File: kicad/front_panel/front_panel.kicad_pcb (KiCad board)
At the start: 2 copper layers, 196.9 x 58.7 mm, 12 parts

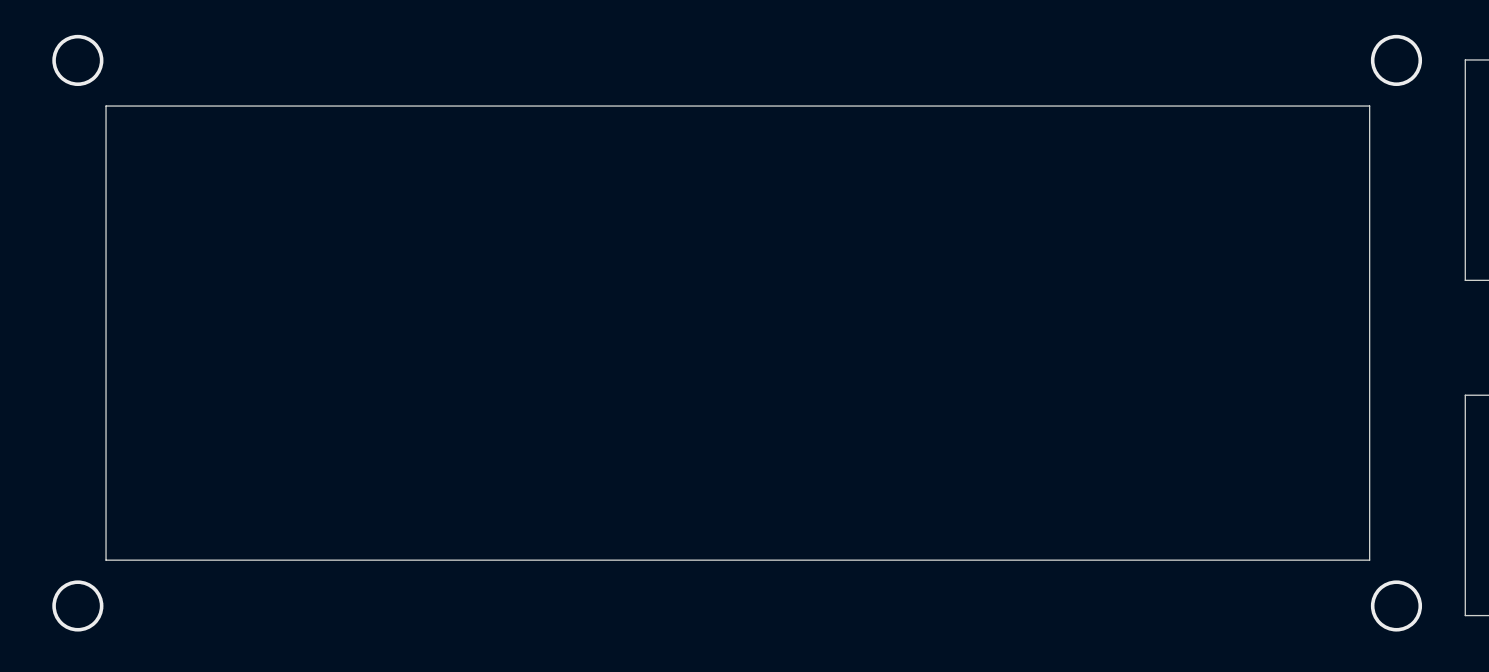
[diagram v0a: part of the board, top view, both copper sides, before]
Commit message: Two small fixups for the display & frontend. Made mounting holes in display PCB larger. Moved LCD window slightly to the right on the front panel.
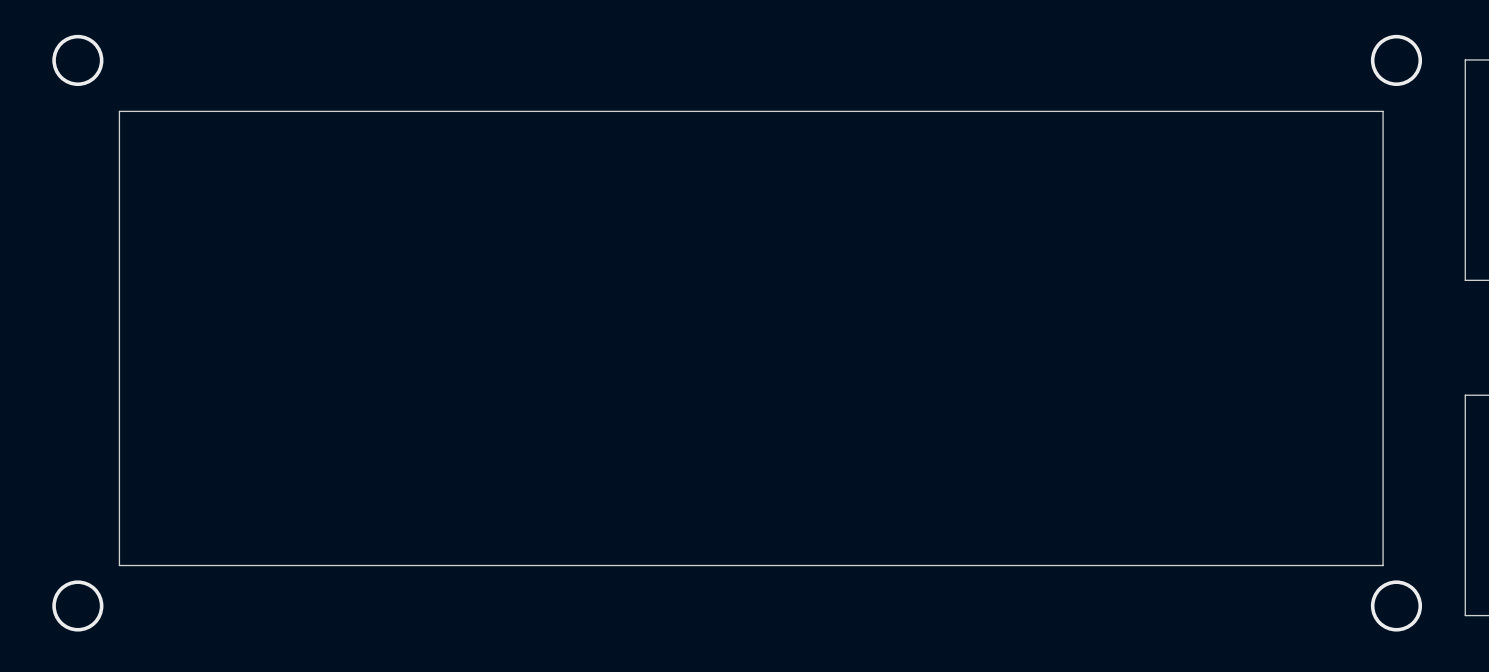
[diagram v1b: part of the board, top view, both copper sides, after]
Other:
- outline, holes or cut-outs redrawn
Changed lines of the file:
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@@
   )
   (paper "A4")
+  (title_block
+    (title "MK312-BT front panel")
+    (date "2022-09-05")
+    (rev "1.4.1-Chi")
+  )
   (layers
     (0 "F.Cu" signal)
@@
   (gr_line (start 157.48 54.6989) (end 162.56 54.6989) (layer "F.SilkS") (width 0.3048))
   (gr_rect (start 134.5184 76.3778) (end 147.0152 88.9) (layer "Edge.Cuts") (width 0.05) (fill none))
-  (gr_rect (start 57.277 59.944) (end 129.0828 85.7504) (layer "Edge.Cuts") (width 0.05) (fill none))
+  (gr_rect (start 58.039 60.2488) (end 129.8448 86.0552) (layer "Edge.Cuts") (width 0.05) (fill none))
   (gr_line (start 50.8 109.5248) (end 50.8 50.8) (layer "Edge.Cuts") (width 0.05))
   (gr_line (start 50.8 50.8) (end 247.65 50.8) (layer "Edge.Cuts") (width 0.05))
